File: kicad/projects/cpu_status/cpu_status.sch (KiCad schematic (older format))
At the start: 115 parts, among them J1 Control_signal_backplane, J2 Aux_connection, J3 Bus_connection, J4 MAR_content_in, J5 Conn_01x03_Male, J6 Conn_01x02_Female, J7 Conn_01x04_Female, U1 74HC245, U11 74HC245, U2 74HC245, U3 74HC245, U4 74HC245, U5 74HC245, U6 74HC245, U7 74HC245, U8 74HC245

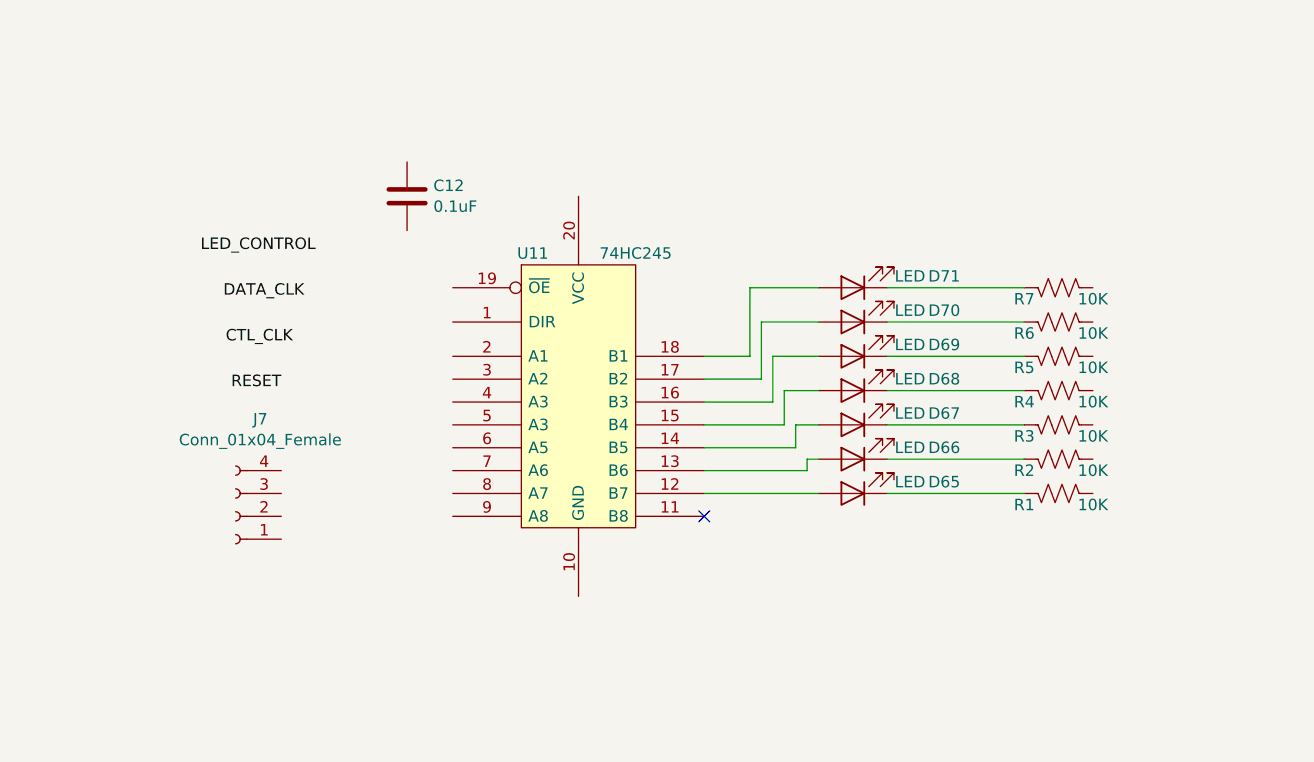
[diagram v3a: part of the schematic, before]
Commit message: Added ECNZ to CPU Status.
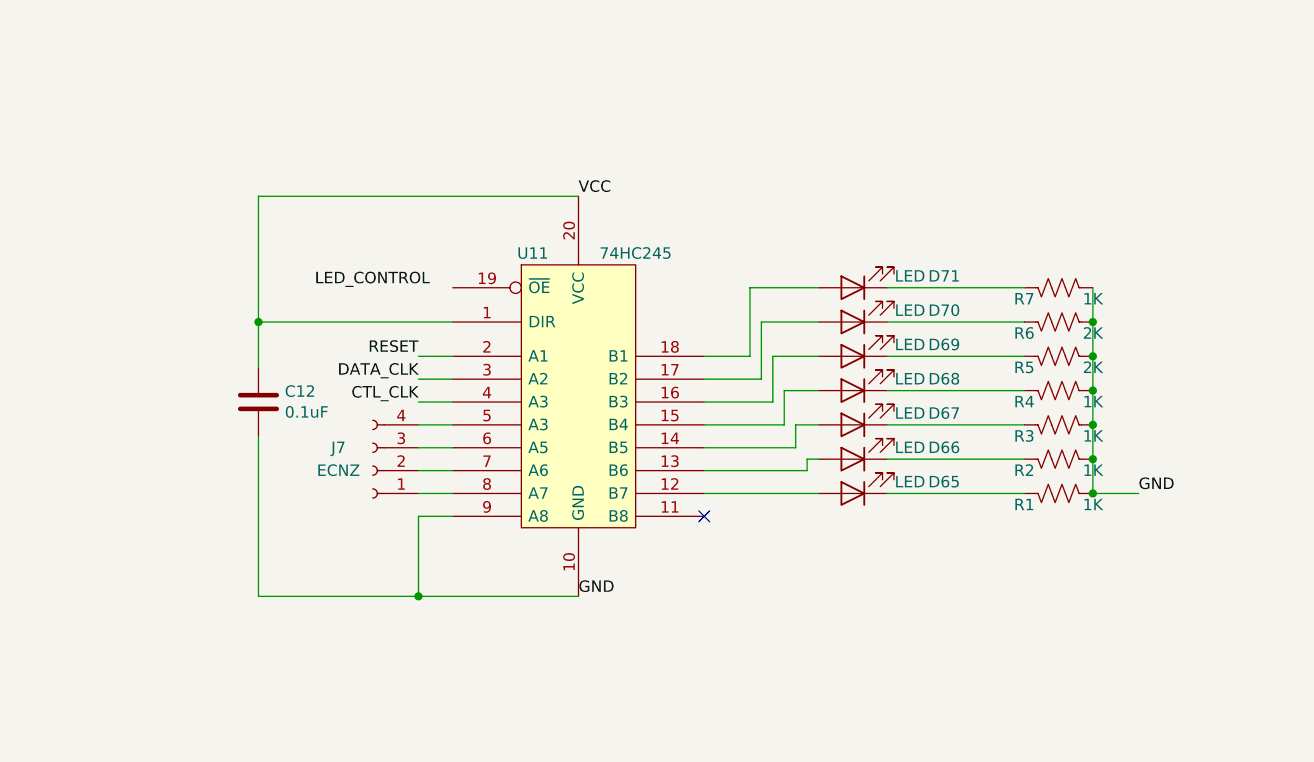
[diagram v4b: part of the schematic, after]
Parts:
- J7: value Conn_01x04_Female -> ECNZ
- R1, R2, R3, R4, R7: value 10K -> 1K
- R5, R6: value 10K -> 2K
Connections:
- net CTL_CLK: now also U11.4 (A3)
- net DATA_CLK: now also U11.3 (A2)
- net GND: now also C12.2, R1.1, R2.1, R3.1, R4.1, R5.1, R6.1, R7.1, U11.10 (GND), U11.9 (A8)
- net RESET: now also U11.2 (A1)
- net VCC: now also C12.1, U11.1 (DIR), U11.20 (VCC)
- net at U11.5 (A3): now also J7.4 (Pin_4)
- net at U11.6 (A5): now also J7.3 (Pin_3)
- net at U11.7 (A6): now also J7.2 (Pin_2)
- net at U11.8 (A7): now also J7.1 (Pin_1)
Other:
- moved on the sheet: C12, J7
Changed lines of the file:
@@
 P 14700 7000
 F 0 "R4" V 14650 6850 50  0000 C CNN
-F 1 "10K" V 14650 7150 50  0000 C CNN
+F 1 "1K" V 14650 7150 50  0000 C CNN
 F 2 "Resistor_THT:R_Axial_DIN0207_L6.3mm_D2.5mm_P2.54mm_Vertical" V 14740 6990 50  0001 C CNN
 F 3 "~" H 14700 7000 50  0001 C CNN
@@
 	1    0    0    -1
 $EndComp
-Text Label 11400 6600 2    50   ~ 0
+Text Label 11900 6950 2    50   ~ 0
 DATA_CLK
-Text Label 11350 6800 2    50   ~ 0
+Text Label 11900 7050 2    50   ~ 0
 CTL_CLK
-Text Label 11300 7000 2    50   ~ 0
+Text Label 11900 6850 2    50   ~ 0
 RESET
 $Comp
@@
 $EndComp
 $Comp
-L Connector:Conn_01x04_Female J7
-U 1 1 64AB9514
-P 11100 7550
-F 0 "J7" H 10992 7125 50  0000 C CNN
-F 1 "Conn_01x04_Female" H 10992 7216 50  0000 C CNN
-F 2 "Connector_PinSocket_2.54mm:PinSocket_1x04_P2.54mm_Horizontal" H 11100 7550 50  0001 C CNN
-F 3 "~" H 11100 7550 50  0001 C CNN
-	1    11100 7550
-	-1   0    0    1
-$EndComp
-$Comp
 L Device:R_US R1
 U 1 1 64B367EB
 P 14700 7450
 F 0 "R1" V 14650 7300 50  0000 C CNN
-F 1 "10K" V 14650 7600 50  0000 C CNN
+F 1 "1K" V 14650 7600 50  0000 C CNN
 F 2 "Resistor_THT:R_Axial_DIN0207_L6.3mm_D2.5mm_P2.54mm_Vertical" V 14740 7440 50  0001 C CNN
 F 3 "~" H 14700 7450 50  0001 C CNN
@@
 P 14700 7300
 F 0 "R2" V 14650 7150 50  0000 C CNN
-F 1 "10K" V 14650 7450 50  0000 C CNN
+F 1 "1K" V 14650 7450 50  0000 C CNN
 F 2 "Resistor_THT:R_Axial_DIN0207_L6.3mm_D2.5mm_P2.54mm_Vertical" V 14740 7290 50  0001 C CNN
 F 3 "~" H 14700 7300 50  0001 C CNN
@@
 P 14700 7150
 F 0 "R3" V 14650 7000 50  0000 C CNN
-F 1 "10K" V 14650 7300 50  0000 C CNN
+F 1 "1K" V 14650 7300 50  0000 C CNN
 F 2 "Resistor_THT:R_Axial_DIN0207_L6.3mm_D2.5mm_P2.54mm_Vertical" V 14740 7140 50  0001 C CNN
 F 3 "~" H 14700 7150 50  0001 C CNN
@@
 P 14700 6850
 F 0 "R5" V 14650 6700 50  0000 C CNN
-F 1 "10K" V 14650 7000 50  0000 C CNN
+F 1 "2K" V 14650 7000 50  0000 C CNN
 F 2 "Resistor_THT:R_Axial_DIN0207_L6.3mm_D2.5mm_P2.54mm_Vertical" V 14740 6840 50  0001 C CNN
 F 3 "~" H 14700 6850 50  0001 C CNN
@@
 P 14700 6700
 F 0 "R6" V 14650 6550 50  0000 C CNN
-F 1 "10K" V 14650 6850 50  0000 C CNN
+F 1 "2K" V 14650 6850 50  0000 C CNN
 F 2 "Resistor_THT:R_Axial_DIN0207_L6.3mm_D2.5mm_P2.54mm_Vertical" V 14740 6690 50  0001 C CNN
 F 3 "~" H 14700 6700 50  0001 C CNN
@@
 P 14700 6550
 F 0 "R7" V 14650 6400 50  0000 C CNN
-F 1 "10K" V 14650 6700 50  0000 C CNN
+F 1 "1K" V 14650 6700 50  0000 C CNN
 F 2 "Resistor_THT:R_Axial_DIN0207_L6.3mm_D2.5mm_P2.54mm_Vertical" V 14740 6540 50  0001 C CNN
 F 3 "~" H 14700 6550 50  0001 C CNN
@@
 	0    1    1    0
 $EndComp
+Text Label 11950 6550 2    50   ~ 0
+LED_CONTROL
+Wire Wire Line
+	13950 7450 14550 7450
+Wire Wire Line
+	14550 7300 13950 7300
+Wire Wire Line
+	13950 7150 14550 7150
+Wire Wire Line
+	14550 7000 13950 7000
+Wire Wire Line
+	13950 6850 14550 6850
+Wire Wire Line
+	14550 6700 13950 6700
+Wire Wire Line
+	13950 6550 14550 6550
+Wire Wire Line
+	13150 7450 13650 7450
+Wire Wire Line
+	13150 7350 13600 7350
+Wire Wire Line
+	13600 7350 13600 7300
+Wire Wire Line
+	13600 7300 13650 7300
+Wire Wire Line
+	13150 7250 13550 7250
+Wire Wire Line
+	13550 7250 13550 7150
+Wire Wire Line
+	13550 7150 13650 7150
+Wire Wire Line
+	13150 7150 13500 7150
+Wire Wire Line
+	13500 7150 13500 7000
+Wire Wire Line
+	13500 7000 13650 7000
+Wire Wire Line
+	13150 7050 13450 7050
+Wire Wire Line
+	13450 7050 13450 6850
+Wire Wire Line
+	13450 6850 13650 6850
+Wire Wire Line
+	13150 6950 13400 6950
+Wire Wire Line
+	13400 6950 13400 6700
+Wire Wire Line
+	13400 6700 13650 6700
+Wire Wire Line
+	13150 6850 13350 6850
+Wire Wire Line
+	13350 6850 13350 6550
+Wire Wire Line
+	13350 6550 13650 6550
+NoConn ~ 13150 7550
+Text Label 12600 7900 0    50   ~ 0
+GND
+Text Label 12600 6150 0    50   ~ 0
+VCC
+Wire Wire Line
+	11900 6850 12050 6850
+Wire Wire Line
+	11900 6950 12050 6950
+Wire Wire Line
+	11900 7050 12050 7050
+Wire Wire Line
+	12050 7150 11900 7150
+Wire Wire Line
+	11900 7250 12050 7250
+Wire Wire Line
+	12050 7350 11900 7350
+Wire Wire Line
+	11900 7450 12050 7450
+Wire Wire Line
+	12600 7900 11900 7900
+Wire Wire Line
+	12050 7550 11900 7550
+Wire Wire Line
+	11900 7550 11900 7900
+$Comp
+L Connector:Conn_01x04_Female J7
+U 1 1 64AB9514
+P 11700 7350
+F 0 "J7" H 11850 7250 50  0000 C CNN
+F 1 "ECNZ" H 11850 7350 50  0000 C CNN
+F 2 "Connector_PinSocket_2.54mm:PinSocket_1x04_P2.54mm_Horizontal" H 11700 7350 50  0001 C CNN
+F 3 "~" H 11700 7350 50  0001 C CNN
+	1    11700 7350
+	-1   0    0    1
+$EndComp
+Connection ~ 11900 7900
+Wire Wire Line
+	11900 7900 11200 7900
+Connection ~ 11200 6700
+Wire Wire Line
+	11200 6150 12600 6150
+Wire Wire Line
+	11200 6700 11200 6150
+Wire Wire Line
+	11200 6700 11200 6900
+Wire Wire Line
+	12050 6700 11200 6700
+Wire Wire Line
+	11200 7900 11200 7200
 $Comp
 L Device:C C12
 U 1 1 64B3B081
-P 11850 6150
-F 0 "C12" H 11965 6196 50  0000 L CNN
-F 1 "0.1uF" H 11965 6105 50  0000 L CNN
-F 2 "Capacitor_THT:C_Disc_D4.7mm_W2.5mm_P5.00mm" H 11888 6000 50  0001 C CNN
-F 3 "~" H 11850 6150 50  0001 C CNN
-	1    11850 6150
+P 11200 7050
+F 0 "C12" H 11315 7096 50  0000 L CNN
+F 1 "0.1uF" H 11315 7005 50  0000 L CNN
+F 2 "Capacitor_THT:C_Disc_D4.7mm_W2.5mm_P5.00mm" H 11238 6900 50  0001 C CNN
+F 3 "~" H 11200 7050 50  0001 C CNN
+	1    11200 7050
 	1    0    0    -1
 $EndComp
-Text Label 11450 6400 2    50   ~ 0
-LED_CONTROL
-Wire Wire Line
-	13950 7450 14550 7450
-Wire Wire Line
-	14550 7300 13950 7300
-Wire Wire Line
-	13950 7150 14550 7150
-Wire Wire Line
-	14550 7000 13950 7000
-Wire Wire Line
-	13950 6850 14550 6850
-Wire Wire Line
-	14550 6700 13950 6700
-Wire Wire Line
-	13950 6550 14550 6550
-Wire Wire Line
-	13150 7450 13650 7450
-Wire Wire Line
-	13150 7350 13600 7350
-Wire Wire Line
-	13600 7350 13600 7300
-Wire Wire Line
-	13600 7300 13650 7300
-Wire Wire Line
-	13150 7250 13550 7250
-Wire Wire Line
-	13550 7250 13550 7150
-Wire Wire Line
-	13550 7150 13650 7150
-Wire Wire Line
-	13150 7150 13500 7150
-Wire Wire Line
-	13500 7150 13500 7000
-Wire Wire Line
-	13500 7000 13650 7000
-Wire Wire Line
-	13150 7050 13450 7050
-Wire Wire Line
-	13450 7050 13450 6850
-Wire Wire Line
-	13450 6850 13650 6850
-Wire Wire Line
-	13150 6950 13400 6950
-Wire Wire Line
-	13400 6950 13400 6700
-Wire Wire Line
-	13400 6700 13650 6700
-Wire Wire Line
-	13150 6850 13350 6850
-Wire Wire Line
-	13350 6850 13350 6550
-Wire Wire Line
-	13350 6550 13650 6550
-NoConn ~ 13150 7550
+Wire Wire Line
+	14850 6550 14850 6700
+Wire Wire Line
+	14850 7450 15050 7450
+Connection ~ 14850 7450
+Connection ~ 14850 6700
+Wire Wire Line
+	14850 6700 14850 6850
+Connection ~ 14850 6850
+Wire Wire Line
+	14850 6850 14850 7000
+Connection ~ 14850 7000
+Wire Wire Line
+	14850 7000 14850 7150
+Connection ~ 14850 7150
+Wire Wire Line
+	14850 7150 14850 7300
+Connection ~ 14850 7300
+Wire Wire Line
+	14850 7300 14850 7450
+Text Label 15050 7450 0    50   ~ 0
+GND
 $EndSCHEMATC

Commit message: Add ustep display to status.
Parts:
- added C13: 0.1uF, Capacitor_THT:C_Disc_D4.7mm_W2.5mm_P5.00mm, symbol Device:C
- added D72, D73, D74: LED, sixteen-bit-computer:LED_D5.0mm, symbol Device:LED
- added Q1: 2N3904, Package_TO_SOT_THT:TO-92L_Inline_Wide, symbol sixteen-bit-computer:2N3904
- added R10, R9: 10K, Resistor_THT:R_Axial_DIN0207_L6.3mm_D2.5mm_P2.54mm_Vertical, symbol Device:R_US
- added R11, R12, R13: 2K, Resistor_THT:R_Axial_DIN0207_L6.3mm_D2.5mm_P2.54mm_Vertical, symbol Device:R_US
- added U9: 74HC126, Package_DIP:DIP-14_W7.62mm, symbol sixteen-bit-computer:74HC126
- J7: footprint Connector_PinSocket_2.54mm:PinSocket_1x04_P2.54mm_Horizontal -> Connector_PinSocket_2.54mm:PinSocket_1x07_P2.54mm_Horizontal; symbol Connector:Conn_01x04_Female -> Connector:Conn_01x07_Female
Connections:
- net GND: now also C13.2, Q1.3 (E), R11.1, R12.1, R13.1, U9.12, U9.13, U9.7 (GND)
- net LED_CONTROL: now also U11.19 (~OE), R9.2
- net VCC: now also C13.1, R10.2, U9.14 (VCC)
- net EQUAL: now reaches J7.4 (Pin_4)
- net EQUAL: now also U11.8 (A7); no longer U11.5 (A3)
- net CLOCK_2: now reaches J7.3 (Pin_3)
- net CLOCK_2: now also U9.9; no longer U11.6 (A5)
- net CARRY: now reaches U11.7 (A6)
- net CARRY: now also J7.5 (Pin_5); no longer J7.2 (Pin_2)
- net CLOCK_0: now reaches J7.1 (Pin_1)
- net CLOCK_0: now also U9.2; no longer U11.8 (A7)
- new net: Q1.1 (C), R10.1, U9.1, U9.10, U9.4
- new net: D72.2 (A), U9.3
- new net: D73.2 (A), U9.6
- new net: D74.2 (A), U9.8
- new net: Q1.2 (B), R9.1
- new net: D72.1 (K), R11.2
- new net: D73.1 (K), R12.2
- new net: D74.1 (K), R13.2
- new net CLOCK_1: J7.2 (Pin_2), U9.5
- new net NEGATIVE: J7.6 (Pin_6), U11.6 (A5)
- new net ZERO: J7.7 (Pin_7), U11.5 (A3)
- no-connect marks 1 -> 2
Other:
- moved on the sheet: C12, D65, D66, D67, D68, D69, D70, D71, R1, R2, R3, R4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

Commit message: Finish adding pull downs to inputs and doing tech checks.
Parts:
- removed R1, R2, R3, R4, R7: 1K, Resistor_THT:R_Axial_DIN0207_L6.3mm_D2.5mm_P2.54mm_Vertical, symbol Device:R_US
- removed R11, R12, R13, R5, R6: 2K, Resistor_THT:R_Axial_DIN0207_L6.3mm_D2.5mm_P2.54mm_Vertical, symbol Device:R_US
- added RN10, RN9: 10K, Resistor_THT:R_Array_SIP5, symbol Device:R_Network04_US
- added RN11, RN13: 2K, Resistor_THT:R_Array_SIP5, symbol Device:R_Network04_US
- added RN12: 1K, Resistor_THT:R_Array_SIP9, symbol Device:R_Network08_US
- RN1, RN2: value R_Network08_US -> 10K
- RN3, RN4: value R_Network08_US -> 2K
- RN5, RN6, RN7, RN8: value R_Network08_US -> 1K
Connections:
- net CARRY: now also RN9.3 (R2)
- net CLOCK_0: now also RN10.3 (R2)
- net CLOCK_1: now also RN10.4 (R3)
- net CLOCK_2: now also RN10.5 (R4)
- net EQUAL: now also RN9.2 (R1)
- net GND: now also RN10.1 (common), RN11.1 (common), RN12.1 (common), RN13.1 (common), RN9.1 (common)
- net NEGATIVE: now also RN9.4 (R3)
- net ZERO: now also RN9.5 (R4)
- net at D68.1 (K): now also RN12.3 (R2)
- net at D65.1 (K): now also RN12.9 (R8)
- net at D66.1 (K): now also RN12.7 (R6)
- net at D67.1 (K): now also RN12.4 (R3)
- net at D69.1 (K): now also RN11.5 (R4)
- net at D70.1 (K): now also RN11.2 (R1)
- net at D71.1 (K): now also RN12.2 (R1)
- net at D72.1 (K): now also RN13.2 (R1)
- net at D73.1 (K): now also RN13.3 (R2)
- net at D74.1 (K): now also RN13.5 (R4)
- no-connect marks 2 -> 9

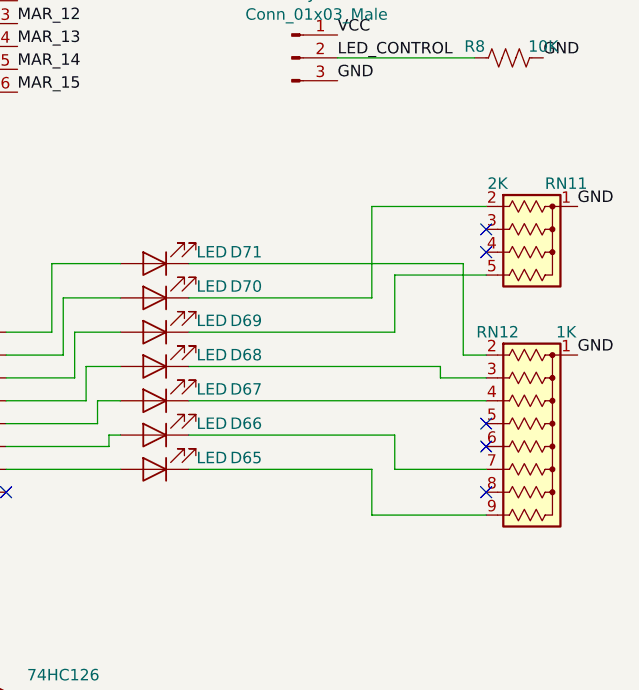
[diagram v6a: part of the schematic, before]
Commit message: Couple of fixes to status - tech checks and adding  micro step output to control uint.
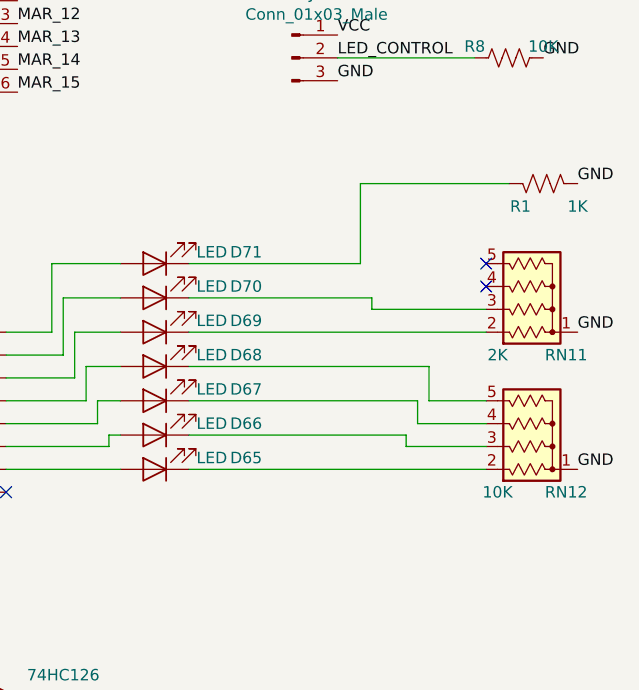
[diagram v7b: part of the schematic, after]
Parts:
- removed RN12: 1K, Resistor_THT:R_Array_SIP9, symbol Device:R_Network08_US
- added R1: 1K, Resistor_THT:R_Axial_DIN0207_L6.3mm_D2.5mm_P10.16mm_Horizontal, symbol Device:R_US
- added RN12: 10K, Resistor_THT:R_Array_SIP5, symbol Device:R_Network04_US
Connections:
- net GND: now also R1.1, RN12.1 (common)
- net at D65.1 (K): now also RN12.2 (R1)
- net at D66.1 (K): now also RN12.3 (R2)
- net at D67.1 (K): now also RN12.4 (R3)
- net at D68.1 (K): now also RN12.5 (R4)
- net at D69.1 (K): now also RN11.2 (R1); no longer RN11.5 (R4)
- net at D70.1 (K): now also RN11.3 (R2); no longer RN11.2 (R1)
- net at D71.1 (K): now also R1.2
- no-connect marks 9 -> 6
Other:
- moved on the sheet: RN11
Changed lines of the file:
@@
 	1    0    0    -1
 $EndComp
-Text Label 15700 5600 0    50   ~ 0
+Text Label 15700 6100 0    50   ~ 0
 GND
 $Comp
@@
 GND
 $Comp
-L Device:R_Network08_US RN12
-U 1 1 66D2EE19
-P 15500 6000
-F 0 "RN12" V 15000 5850 50  0000 C CNN
-F 1 "1K" V 15000 6150 50  0000 C CNN
-F 2 "Resistor_THT:R_Array_SIP9" V 15975 6000 50  0001 C CNN
-F 3 "http://www.vishay.com/docs/31509/csc.pdf" H 15500 6000 50  0001 C CNN
-	1    15500 6000
-	0    1    1    0
-$EndComp
-$Comp
 L Device:R_Network04_US RN11
 U 1 1 66DCDAA7
-P 15500 5150
-F 0 "RN11" V 15200 5300 50  0000 C CNN
-F 1 "2K" V 15200 5000 50  0000 C CNN
-F 2 "Resistor_THT:R_Array_SIP5" V 15775 5150 50  0001 C CNN
-F 3 "http://www.vishay.com/docs/31509/csc.pdf" H 15500 5150 50  0001 C CNN
-	1    15500 5150
-	0    1    1    0
-$EndComp
-Wire Wire Line
-	14800 6100 14800 6300
-Wire Wire Line
-	14800 6300 15300 6300
-Wire Wire Line
-	14000 6100 14800 6100
-Wire Wire Line
-	14000 5950 14900 5950
-Wire Wire Line
-	14000 5650 15100 5650
-Wire Wire Line
-	15200 5200 15200 5600
-Wire Wire Line
-	15200 5600 15300 5600
-Wire Wire Line
-	14000 5200 15200 5200
-Wire Wire Line
-	14800 5350 14800 4950
-Wire Wire Line
-	14800 4950 15300 4950
+P 15500 5300
+F 0 "RN11" V 15200 5450 50  0000 C CNN
+F 1 "2K" V 15200 5150 50  0000 C CNN
+F 2 "Resistor_THT:R_Array_SIP5" V 15775 5300 50  0001 C CNN
+F 3 "http://www.vishay.com/docs/31509/csc.pdf" H 15500 5300 50  0001 C CNN
+	1    15500 5300
+	0    1    -1   0
+$EndComp
+Wire Wire Line
+	14800 5350 14800 5400
 Wire Wire Line
 	14000 5350 14800 5350
-Wire Wire Line
-	14900 5500 14900 5250
-Wire Wire Line
-	14000 5500 14900 5500
-Text Label 15700 4950 0    50   ~ 0
-GND
-NoConn ~ 15300 5150
-NoConn ~ 15300 5900
-Wire Wire Line
-	14900 5950 14900 6100
-Wire Wire Line
-	14900 6100 15300 6100
-Wire Wire Line
-	14000 5800 15300 5800
-Wire Wire Line
-	15100 5650 15100 5700
-Wire Wire Line
-	15100 5700 15300 5700
-NoConn ~ 15300 6200
-NoConn ~ 15300 6000
-Wire Wire Line
-	15300 5250 14900 5250
-NoConn ~ 15300 5050
+Text Label 15700 4850 0    50   ~ 0
+GND
+Wire Wire Line
+	14000 5800 15000 5800
+NoConn ~ 15300 5300
 $Comp
 L Device:R_Network04_US RN13
@@
 	13900 7200 14550 7200
 NoConn ~ 14700 7900
+$Comp
+L Device:R_Network04_US RN12
+U 1 1 678D945A
+P 15500 5900
+F 0 "RN12" V 15200 6050 50  0000 C CNN
+F 1 "10K" V 15200 5750 50  0000 C CNN
+F 2 "Resistor_THT:R_Array_SIP5" V 15775 5900 50  0001 C CNN
+F 3 "http://www.vishay.com/docs/31509/csc.pdf" H 15500 5900 50  0001 C CNN
+	1    15500 5900
+	0    1    -1   0
+$EndComp
+Wire Wire Line
+	14000 6100 15300 6100
+Wire Wire Line
+	15300 6000 14950 6000
+Wire Wire Line
+	14950 6000 14950 5950
+Wire Wire Line
+	14000 5950 14950 5950
+Wire Wire Line
+	15000 5800 15000 5900
+Wire Wire Line
+	15000 5900 15300 5900
+Wire Wire Line
+	15300 5800 15050 5800
+Wire Wire Line
+	14000 5650 15050 5650
+Wire Wire Line
+	15050 5650 15050 5800
+$Comp
+L Device:R_US R1
+U 1 1 67C06FB5
+P 15550 4850
+F 0 "R1" V 15450 4750 50  0000 C CNN
+F 1 "1K" V 15450 5000 50  0000 C CNN
+F 2 "Resistor_THT:R_Axial_DIN0207_L6.3mm_D2.5mm_P10.16mm_Horizontal" V 15590 4840 50  0001 C CNN
+F 3 "~" H 15550 4850 50  0001 C CNN
+	1    15550 4850
+	0    1    -1   0
+$EndComp
+Wire Wire Line
+	14000 5500 15300 5500
+Text Label 15700 5500 0    50   ~ 0
+GND
+Wire Wire Line
+	14000 5200 14750 5200
+Wire Wire Line
+	14750 5200 14750 4850
+Wire Wire Line
+	14750 4850 15400 4850
+NoConn ~ 15300 5200
+Wire Wire Line
+	14800 5400 15300 5400
 $EndSCHEMATC
